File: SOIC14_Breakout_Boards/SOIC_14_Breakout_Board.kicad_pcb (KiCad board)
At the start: 2 copper layers, 25 x 25 mm, 6 parts, among them J1 Conn_01x04, J2 Conn_01x04, J3 Conn_01x01, J4 Conn_01x01

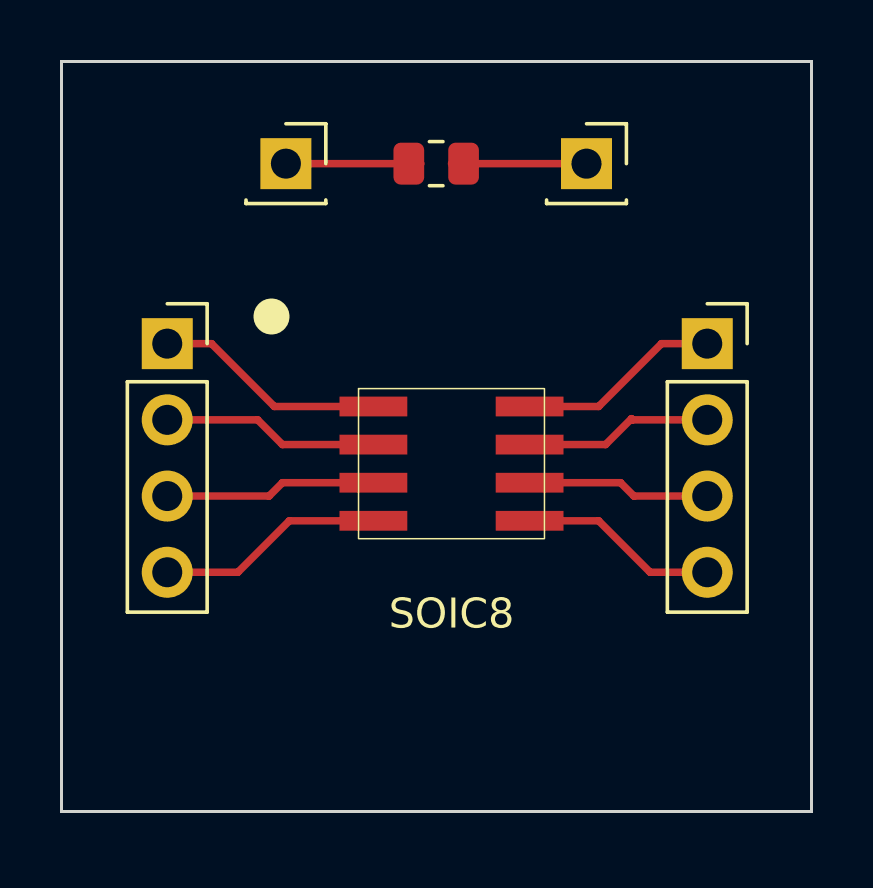
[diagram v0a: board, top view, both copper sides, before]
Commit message: Created PCB designs for the 14, 16 & 20 pic SOIC's
Finalized and committed pcb designs for the 14, 16, and 20 SOIC breakout boards
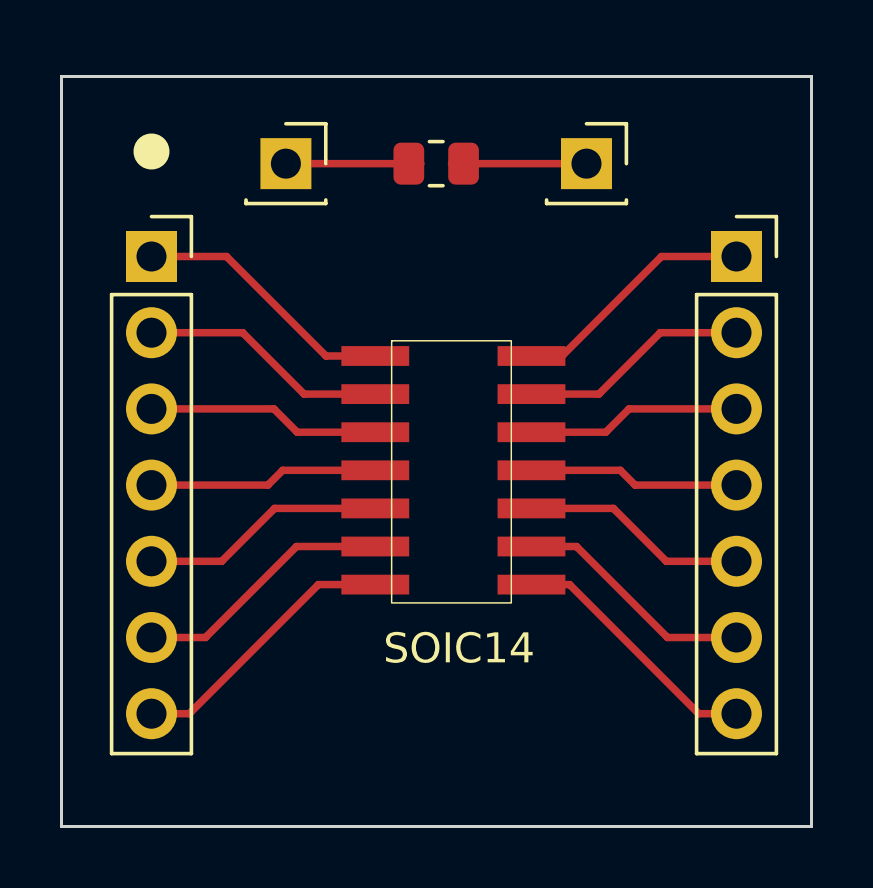
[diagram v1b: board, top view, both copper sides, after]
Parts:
- removed SOIC8: 8_Pin_SOIC_Board, SOIC_Footprints:8_Pin_SOIC_Board
- added SOIC14: 14_Pin_SOIC_Board, SOIC_Footprints:14_Pin_SOIC_Board, F.Cu at (155.1, 101.5)
- J1, J2: value Conn_01x04 -> Conn_01x07; footprint Connector_PinSocket_2.54mm:PinSocket_1x04_P2.54mm_Vertical -> Connector_PinSocket_2.54mm:PinSocket_1x07_P2.54mm_Vertical
- moved J2 3.06 mm to (164.5, 94.5)
- moved J1 2.95 mm to (145.0, 94.5)
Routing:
- net Net-(J1-Pad7): track 0.00 -> 9.24 mm
- net Net-(J1-Pad6): track 0.00 -> 8.72 mm
- net Net-(J2-Pad7): track 0.00 -> 8.62 mm
- net Net-(J1-Pad5): track 0.00 -> 8.19 mm
- net Net-(J2-Pad6): track 0.00 -> 8.09 mm
- net Net-(J2-Pad5): track 0.00 -> 7.56 mm
- net Net-(J1-Pad2): track 6.71 -> 8.31 mm
- net Net-(J1-Pad1): track 7.24 -> 8.83 mm
- net Net-(J1-Pad3): track 6.56 -> 7.78 mm
- net Net-(J2-Pad1): track 7.29 -> 8.21 mm
- net Net-(J2-Pad2): track 6.80 -> 7.68 mm
- net Net-(J1-Pad4): track 7.08 -> 7.66 mm
- net Net-(J2-Pad3): track 6.61 -> 7.16 mm
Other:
- board text added: "14 Pin SOIC Breakout Board"
- board text removed: "8 Pin SOIC Breakout Board"

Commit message: Fixed warnings on all SOIC boards
Ensured that silkscreen traces didn't intersect solder masks and name/board information is visible on the front of the board rather than the back
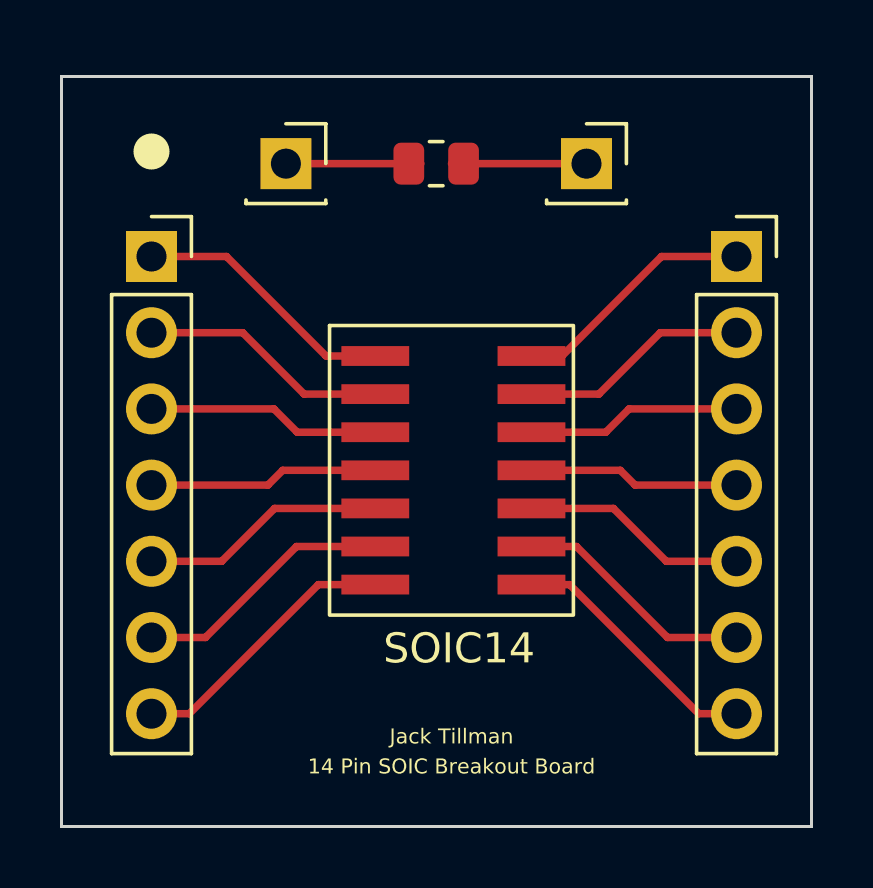
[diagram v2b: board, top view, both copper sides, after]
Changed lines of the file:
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@@
       (effects (font (size 1 1) (thickness 0.15)))
     )
-    (fp_rect (start -2.1209 -4.191) (end 1.8669 4.5466) (layer "F.SilkS") (width 0.05) (fill none))
-    (fp_rect (start -4.191 -4.699) (end 3.937 4.953) (layer "F.Fab") (width 0.12) (fill none))
+    (fp_rect (start -4.191 -4.699) (end 3.937 4.953) (layer "F.SilkS") (width 0.12) (fill none))
+    (fp_rect (start -2.1209 -4.191) (end 1.8669 4.5466) (layer "F.Fab") (width 0.05) (fill none))
     (pad "1" smd rect (at -2.667 -3.683) (size 2.2606 0.6604) (layers "F.Cu" "F.Paste" "F.Mask")
       (net 1 "Net-(J1-Pad1)") (pintype "unspecified"))
@@
   (gr_circle (center 145 91) (end 145.5 91) (layer "F.SilkS") (width 0.2) (fill solid))
   (gr_rect (start 142 88.5) (end 167 113.5) (layer "Edge.Cuts") (width 0.1) (fill none))
-  (gr_text "14 Pin SOIC Breakout Board" (at 155 111.5) (layer "B.SilkS")
+  (gr_text "14 Pin SOIC Breakout Board" (at 155 111.5) (layer "F.SilkS")
     (effects (font (size 0.5 0.5) (thickness 0.05)))
   )
-  (gr_text "Jack Tillman" (at 155.5 110.5) (layer "B.SilkS")
+  (gr_text "Jack Tillman" (at 155 110.5) (layer "F.SilkS")
     (effects (font (size 0.5 0.5) (thickness 0.05)))
   )

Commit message: Finished tracing the SOIC20 board
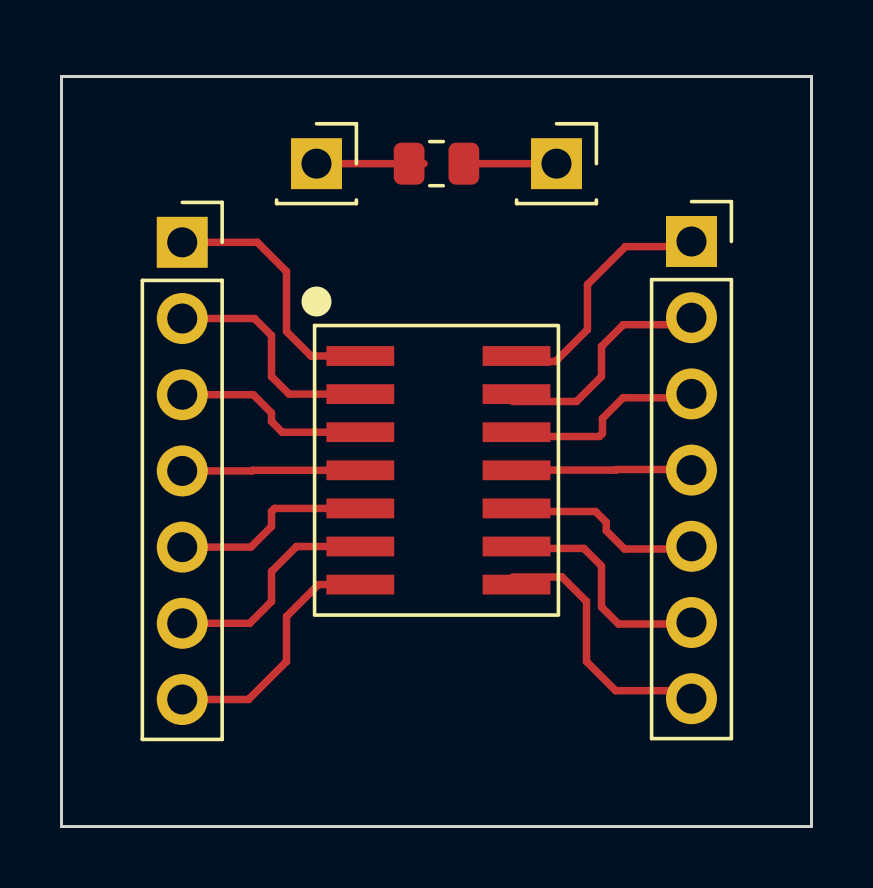
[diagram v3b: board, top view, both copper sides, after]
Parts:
- moved J2 1.58 mm to (163.0, 94.0)
- moved J1 1.13 mm to (146.0, 94.0)
- moved J4 1.02 mm to (150.5, 91.4)
- moved J3 1.00 mm to (158.5, 91.4)
- moved SOIC14 0.50 mm to (154.6, 101.5)
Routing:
- net Net-(J1-Pad4): track 7.66 -> 5.94 mm
- net Net-(J1-Pad5): track 8.19 -> 6.76 mm
- net Net-(J4-Pad1): track 4.50 -> 3.09 mm
- net Net-(J1-Pad3): track 7.78 -> 6.62 mm
- net Net-(J1-Pad6): track 8.72 -> 7.58 mm
- net Net-(J2-Pad4): track 7.04 -> 5.94 mm
- net Net-(J2-Pad5): track 7.56 -> 6.62 mm
- net Net-(J3-Pad1): track 3.98 -> 3.09 mm
- net Net-(J1-Pad7): track 9.24 -> 8.40 mm
- net Net-(J1-Pad2): track 8.31 -> 7.78 mm
